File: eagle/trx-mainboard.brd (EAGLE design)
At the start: 97.6 x 84.5 mm, 31 parts, among them J1 629722000214

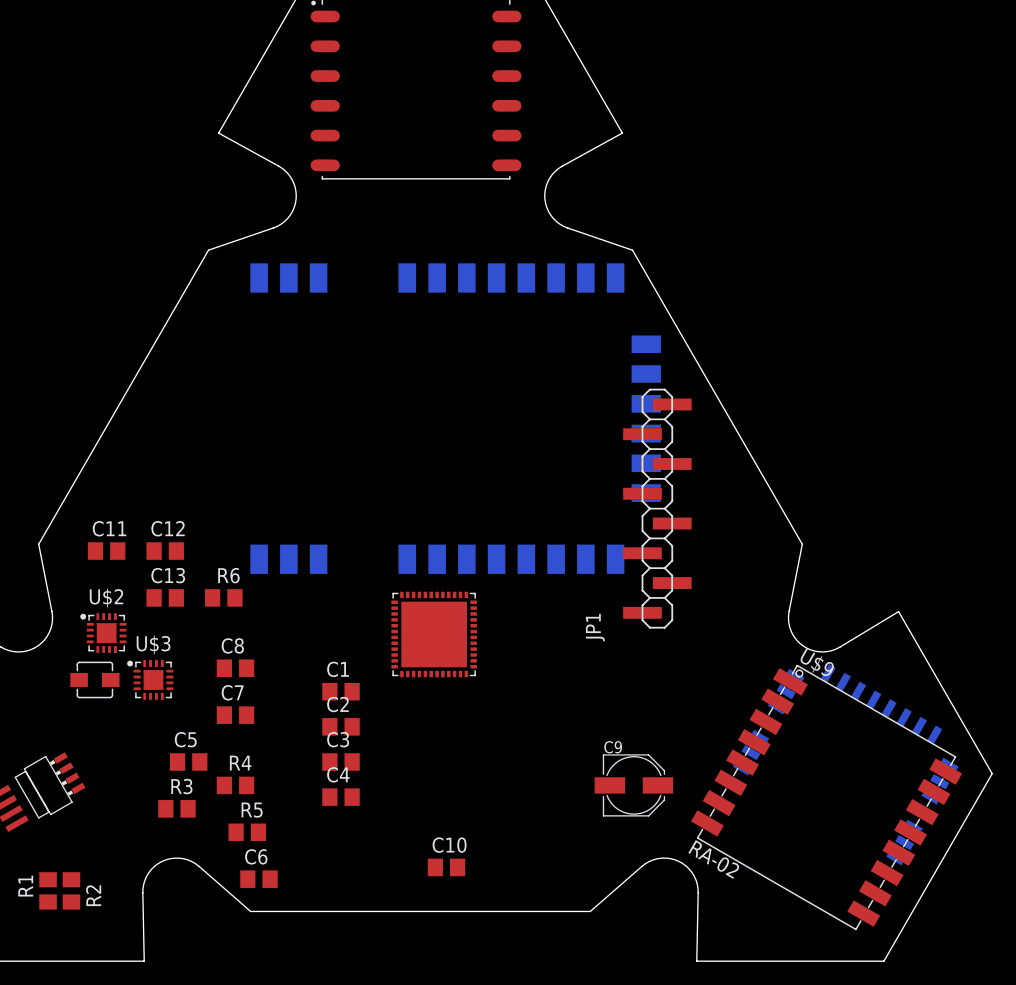
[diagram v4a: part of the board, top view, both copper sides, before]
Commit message: Added breakout board and progressed mainboard
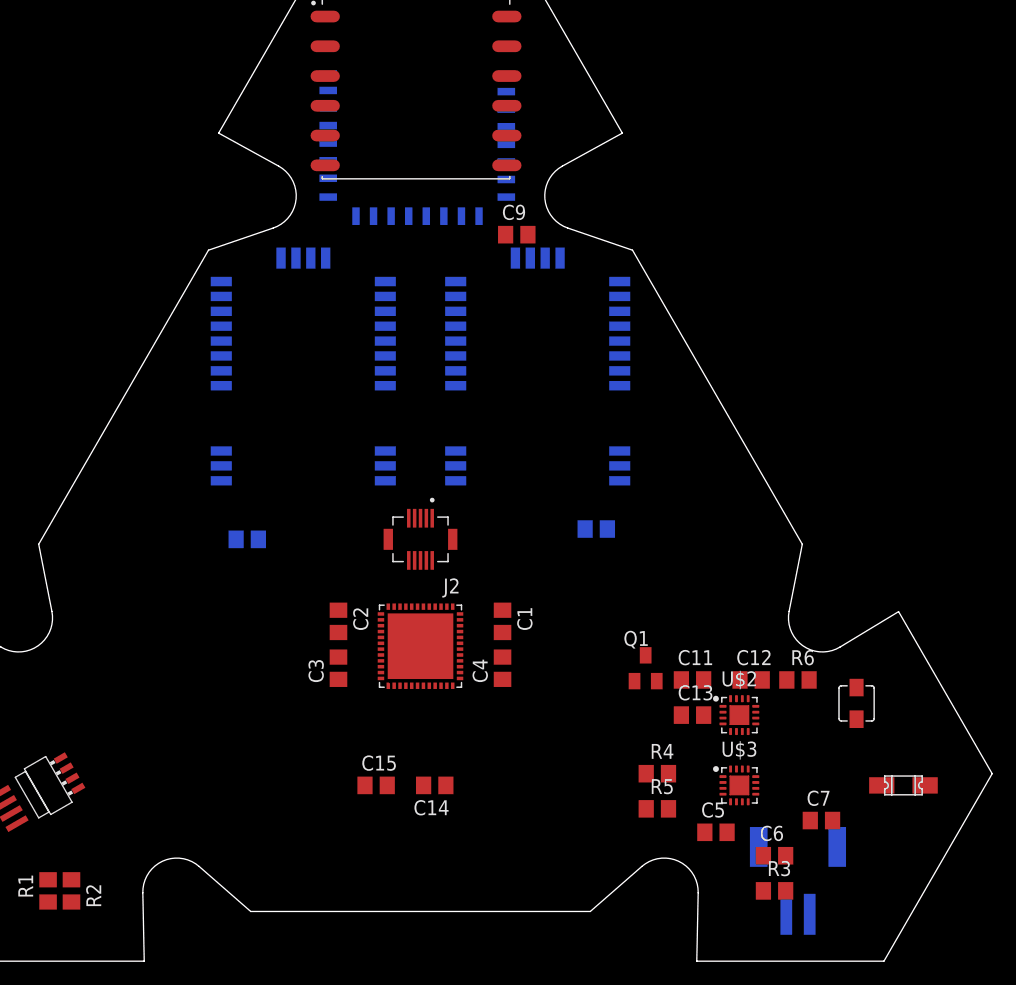
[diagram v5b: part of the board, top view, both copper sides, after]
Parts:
- removed JP1: (no value), pinhead2:1X08SMD
- added C14, C15: 100nF, rcl:C0805
- added F1: 1206L, ptc-littlefuse:1206L
- added J2: DF12NB(3.0)-10DP-0.5V, con-hirose2:HRS_DF12NB(3.0)-10DP-0.5V
- added P1: S2B-PH-SM4-TB, con-jst2:JST_S2B-PH-SM4-TB
- added Q1: BSS84, transistor-small-signal:SOT23
- C9: value (none) -> 100nF; device rcl:PANASONIC_C -> rcl:C0805
- U$6: value E32-900M30S -> E32-X00M20S; device ebyte:E32-900M30S -> ebyte:E32-X00M20S
- U$9: value RA-02 -> E32-X00M20S; device ai-thinker:RA-01/RA-02 -> ebyte:E32-X00M20S
- moved U$5 69.5 mm to (48.5, 73.5), turned to 90 degrees
- moved U$4 65.0 mm to (86.0, 22.0), turned to 90 degrees
- moved U$2 54.5 mm to (76.0, 21.0)
- moved R3 51.5 mm to (79.0, 6.00)
- moved C11 51.2 mm to (72.0, 24.0)
- moved C12 51.2 mm to (77.0, 24.0)
- moved C7 50.8 mm to (83.0, 12.0)
- moved U$3 50.8 mm to (76.0, 15.0)
- moved R6 49.5 mm to (81.0, 24.0)
- moved C9 48.1 mm to (57.0, 62.0)
- moved C13 46.1 mm to (72.0, 21.0)
- moved C5 45.4 mm to (74.0, 11.0)
- moved C6 44.0 mm to (79.0, 9.00)
- moved U$9 43.7 mm to (58.8, 50.0), flipped to the bottom, turned to 0 degrees
- moved R4 36.0 mm to (69.0, 16.0)
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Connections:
- new net LED_RGB_B: J2.7
- new net LED_RGB_G: J2.5
- new net LED_RGB_R: J2.3
- new net LORA1_RXEN: U$10.43, U$9.6
- new net LORA1_TXEN: U$10.42, U$9.7
- new net N$11: C14.2, U$10.7
- new net N$12: F1.P$2, P1.1
- new net N$9: C5.1, Q1.3, U$3.10, U$3.11, U$3.6
- new net PWR_TRIG: J2.4, Q1.1
- net +3V3: now also C15.2, C9.1, U$1.10, U$1.4, U$1.5, U$5.1, U$5.23, U$9.9; no longer C9.+, U$6.10, U$9.3
- net BT_RX: now also U$5.20
- net BT_TX: now also U$5.19
- net GND: now also C14.1, C15.1, C9.2, J2.10, J2.9, P1.2, U$1.12, U$1.3, U$10.44, U$5.24, U$6.10, U$6.16, U$6.24, U$9.10, U$9.11, U$9.12, U$9.24, U$9.26, U$9.3, U$9.4, U$9.5; no longer C9.-, U$6.17, U$6.18, U$6.28, U$9.9
- net GPS_RX: now also U$1.1
- net GPS_TX: now also U$1.2
- net LORA1_D0: now also U$9.18; no longer U$9.5
- net LORA1_MISO: now also U$9.20; no longer U$9.13
- net LORA1_MOSI: now also U$9.21; no longer U$9.14
- net LORA1_RST: now also U$9.19; no longer U$9.4
- net LORA1_SCK: now also U$9.22; no longer U$9.12
- net LORA1_SSEL: now also U$9.23; no longer U$9.15
- net LORA2_D0: now also U$6.18; no longer U$6.20
- net LORA2_MISO: now also U$6.20; no longer U$6.22
- net LORA2_MOSI: now also U$6.21; no longer U$6.23
- net LORA2_RST: now also U$6.19; no longer U$6.21
- net LORA2_SCK: now also U$6.22; no longer U$6.24
- net LORA2_SSEL: now also U$6.23; no longer U$6.25
- net V+: now also Q1.2; no longer C5.1, U$3.10, U$3.11, U$3.6
- net VBAT+: now also F1.P$1, J2.1, J2.2

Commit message: Added basic auto-route
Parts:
- removed U$3: BQ2407X, texas-instruments:VQFN16-3X3
- removed U$7: BC034-04-A-V-0150-L-C, con-gct:P-1X4/90-1.00X1.50MM-SMT
- removed U$8: BC075-04-A-L-A, con-gct:S-1X4/90-1.00MM-SMT
- added JP1: (no value), pinhead2:1X04SMD
- added U$11: BG230-04, con-gct:S-1X4/90-2.54MM-SMT
- added U$12: BG035-04, con-gct:P-1X4/90-2.54X1.50MM-SMT
- added U2: BQ2407X, texas-instruments:VQFN16-3X3
- moved C11 16.3 mm to (87.5, 19.0), turned to 90 degrees
- moved P1 16.0 mm to (80.0, 20.0), turned to 90 degrees
- moved R4 15.9 mm to (79.5, 4.00), turned to 90 degrees
- moved R1 15.9 mm to (5.50, 17.0), turned to 210 degrees
- moved Q1 13.0 mm to (75.0, 14.0), turned to 90 degrees
- moved R6 11.9 mm to (87.5, 14.0), turned to 270 degrees
- moved C5 11.8 mm to (83.5, 4.00), turned to 270 degrees
- moved C13 11.7 mm to (83.5, 19.0), turned to 90 degrees
- moved R5 11.1 mm to (75.5, 4.00), turned to 270 degrees
- moved U$4 10.9 mm to (75.5, 19.0), turned to 270 degrees
- moved U$2 8.90 mm to (81.5, 14.0)
- moved R3 8.73 mm to (87.5, 4.00), turned to 90 degrees
- moved C8 7.95 mm to (28.8, 42.0), turned to 90 degrees
- moved C10 7.16 mm to (68.8, 42.0), turned to 90 degrees
- moved R2 6.32 mm to (13.0, 4.00), turned to 210 degrees
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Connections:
- net +3V3: now also JP1.1
- net GND: now also JP1.4, U$11.1, U2.14, U2.15, U2.17, U2.4, U2.5, U2.8; no longer U$3.14, U$3.15, U$3.17, U$3.4, U$3.5, U$3.8, U$8.1
- net N$3: now also U2.12; no longer U$3.12
- net N$4: now also U2.16; no longer U$3.16
- net N$5: now also U2.1; no longer U$3.1
- net N$9: now also U2.10, U2.11, U2.6; no longer U$3.10, U$3.11, U$3.6
- net SWCLK: now also JP1.3
- net SWDIO: now also JP1.2
- net USB_D+: now also U$12.3; no longer U$7.3
- net USB_D-: now also U$12.2; no longer U$7.2
- net USB_DM: now also U$11.2; no longer U$8.2
- net USB_DP: now also U$11.3; no longer U$8.3
- net USB_GND: now also U$12.1; no longer U$7.1
- net USB_V: now also U$12.4; no longer U$7.4
- net VBAT+: now also U2.2, U2.3; no longer U$3.2, U$3.3
- net VUSB: now also U$11.4, U2.13; no longer U$3.13, U$8.4
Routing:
- net GND: track 0.00 -> 453.0 mm, vias 0 -> 13
- net +3V3: track 0.00 -> 261.2 mm, vias 0 -> 7
- net VBAT+: track 0.00 -> 84.8 mm, vias 0 -> 2
- net LORA1_TXEN: track 0.00 -> 62.7 mm, vias 0 -> 1
- net VUSB: track 0.00 -> 61.8 mm, vias 0 -> 2
- net LORA1_RXEN: track 0.00 -> 60.1 mm, vias 0 -> 3
- net BT_RX: track 0.00 -> 60.1 mm, vias 0 -> 3
- net BT_TX: track 0.00 -> 55.7 mm, vias 0 -> 3
- net GPS_RX: track 0.00 -> 55.3 mm, vias 0 -> 2
- net GPS_TX: track 0.00 -> 51.1 mm
- net LORA1_D0: track 0.00 -> 47.4 mm, vias 0 -> 3
- net SWCLK: track 0.00 -> 44.1 mm, vias 0 -> 2
- net PWR_TRIG: track 0.00 -> 43.5 mm, vias 0 -> 2
- net LORA2_RST: track 0.00 -> 43.5 mm, vias 0 -> 1
- net USB_GND: track 0.00 -> 41.0 mm
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
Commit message: Finalized alpha design
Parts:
- removed U$12: BG035-04, con-gct:P-1X4/90-2.54X1.50MM-SMT
- added R7: 33R, rcl:R0805
- added U$3: BG080-04, con-gct:P-1X4/90-2.54X1.50MMX2.54MM-SMT
- moved R5 44.9 mm to (43.0, 35.0)
- moved C6 43.5 mm to (51.0, 45.0), turned to 90 degrees
- moved R6 40.5 mm to (61.5, 45.0)
- moved C7 36.8 mm to (61.5, 35.0)
- moved R3 36.8 mm to (61.5, 30.0)
- moved C13 36.4 mm to (58.0, 45.0)
- moved C5 36.4 mm to (58.0, 30.0)
- moved Q1 36.2 mm to (42.5, 30.0), turned to 180 degrees
- moved C12 36.1 mm to (54.5, 45.0)
- moved R4 36.1 mm to (54.5, 30.0)
- moved U$2 36.1 mm to (56.5, 40.0)
- moved U2 36.1 mm to (56.5, 35.0)
- moved C11 33.4 mm to (61.5, 40.0)
- moved U$4 32.3 mm to (51.0, 40.0), turned to 90 degrees
- moved C14 18.5 mm to (36.0, 35.0)
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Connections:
- removed net LED_RGB_B: J2.7
- removed net LED_RGB_G: J2.5
- removed net LED_RGB_R: J2.3
- new net LED_D: J2.3, R7.1
- net +3V3: now also J2.1, U$10.36
- net GND: now also U$2.15, U$2.16, U$2.17, U$2.5, U$2.6
- net N$10: now also R7.2, U$10.40; no longer U$2.15, U$2.16, U$2.17, U$2.5, U$2.6
- net N$9: now also Q1.2; no longer Q1.3
- net USB_D+: now also U$3.3; no longer U$12.3
- net USB_D-: now also U$3.2; no longer U$12.2
- net USB_GND: now also U$3.1; no longer U$12.1
- net USB_V: now also U$3.4; no longer U$12.4
- net V+: now also Q1.3; no longer Q1.2
- net VBAT+: no longer J2.1
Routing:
- net GND: track 453.0 -> 389.4 mm, vias 13 -> 11
- net LORA1_TXEN: track 62.7 -> 22.9 mm
- net LORA1_RXEN: track 60.1 -> 21.5 mm, vias 3 -> 1
- net PWR_TRIG: track 43.5 -> 6.96 mm, vias 2 -> 0
- net LORA2_RST: track 43.5 -> 9.31 mm
- net VBAT+: track 84.8 -> 59.3 mm
- net SWDIO: track 35.4 -> 60.1 mm
- net LORA2_RXEN: track 38.7 -> 14.4 mm
- net N$8: track 8.61 -> 30.7 mm
- net +3V3: track 261.2 -> 239.2 mm, vias 7 -> 13
- net LORA2_SCK: track 29.6 -> 8.65 mm
- net LORA2_TXEN: track 34.7 -> 14.6 mm, vias 3 -> 1
- net LORA2_SSEL: track 24.7 -> 5.12 mm
- net LORA2_D0: track 33.1 -> 14.1 mm, vias 1 -> 3
- net LORA2_MOSI: track 25.8 -> 7.79 mm
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- added copper zone on layer 1, net GND
- added copper zone on layer 16, net GND
- added copper zone on layer 1, net USB_GND
- added copper zone on layer 16, net USB_GND
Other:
- outline, holes or cut-outs redrawn
- board text added: "CLK"
- board text added: "DIO"
- board text added: "GND"
- board text added: "VCC"

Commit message: Added new layout and gerber files
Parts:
- removed U$6, U$9: E32-X00M20S, ebyte:E32-X00M20S
- added LORA1, LORA2: E32-X00M20S, ebyte:E32-X00M20S
- C11: value 100nF -> 10uF
- C12: value 100nF -> 3.3nF
- R4: value 3k -> 1.8k
- R5: value 3k -> 10k
- R6: value 3k -> 100k
- moved U$1 0.50 mm to (48.9, 74.3)
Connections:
- net +3V3: now also LORA1.9, LORA2.9; no longer U$6.9, U$9.9
- net GND: now also LORA1.1, LORA1.10, LORA1.11, LORA1.12, LORA1.16, LORA1.2, LORA1.24, LORA1.26, LORA1.3, LORA1.4, LORA1.5, LORA2.1, LORA2.10, LORA2.11, LORA2.12, LORA2.16, LORA2.2, LORA2.24, LORA2.26, LORA2.3, LORA2.4, LORA2.5; no longer U$6.1, U$6.10, U$6.11, U$6.12, U$6.16, U$6.2, U$6.24, U$6.26, U$6.3, U$6.4, U$6.5, U$9.1, U$9.10, U$9.11, U$9.12, U$9.16, U$9.2, U$9.24, U$9.26, U$9.3, U$9.4, U$9.5
- net LORA1_D0: now also LORA1.18; no longer U$9.18
- net LORA1_MISO: now also LORA1.20; no longer U$9.20
- net LORA1_MOSI: now also LORA1.21; no longer U$9.21
- net LORA1_RST: now also LORA1.19; no longer U$9.19
- net LORA1_RXEN: now also LORA1.6; no longer U$9.6
- net LORA1_SCK: now also LORA1.22; no longer U$9.22
- net LORA1_SSEL: now also LORA1.23; no longer U$9.23
- net LORA1_TXEN: now also LORA1.7; no longer U$9.7
- net LORA2_D0: now also LORA2.18; no longer U$6.18
- net LORA2_MISO: now also LORA2.20; no longer U$6.20
- net LORA2_MOSI: now also LORA2.21; no longer U$6.21
- net LORA2_RST: now also LORA2.19; no longer U$6.19
- net LORA2_RXEN: now also LORA2.6; no longer U$6.6
- net LORA2_SCK: now also LORA2.22; no longer U$6.22
- net LORA2_SSEL: now also LORA2.23; no longer U$6.23
- net LORA2_TXEN: now also LORA2.7; no longer U$6.7
- net USB_GND: now also U$3.4; no longer U$3.1
- net USB_V: now also U$3.1; no longer U$3.4
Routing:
- net BT_RX: track 75.4 -> 48.3 mm
- net GPS_TX: track 53.7 -> 39.3 mm
- net GND: track 389.4 -> 376.0 mm
- net N$6: track 5.56 -> 13.3 mm
- net LORA1_TXEN: track 22.9 -> 15.4 mm
- net N$2: track 9.26 -> 1.80 mm, vias 2 -> 0
- net USB_D+: track 11.4 -> 4.76 mm, vias 1 -> 0
- net USB_GND: track 41.5 -> 35.6 mm
- net USB_V: track 17.6 -> 12.3 mm, vias 1 -> 0
- net USB_D-: track 10.8 -> 5.64 mm, vias 1 -> 0
- net V+: track 31.6 -> 36.1 mm
- net GPS_RX: track 45.6 -> 41.7 mm
- net LORA1_RXEN: track 21.5 -> 17.7 mm
- net +3V3: track 239.2 -> 235.9 mm
- net VUSB: track 45.6 -> 48.2 mm
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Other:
- board size 97.6 x 84.5 mm -> 95.3 x 82.5 mm
- board text added: "LORA1"
- board text added: "LORA2"
